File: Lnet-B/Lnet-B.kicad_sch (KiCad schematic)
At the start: 13 parts, among them J601 RJ12, J602 RJ12, Q601 BC847, U601 LM311

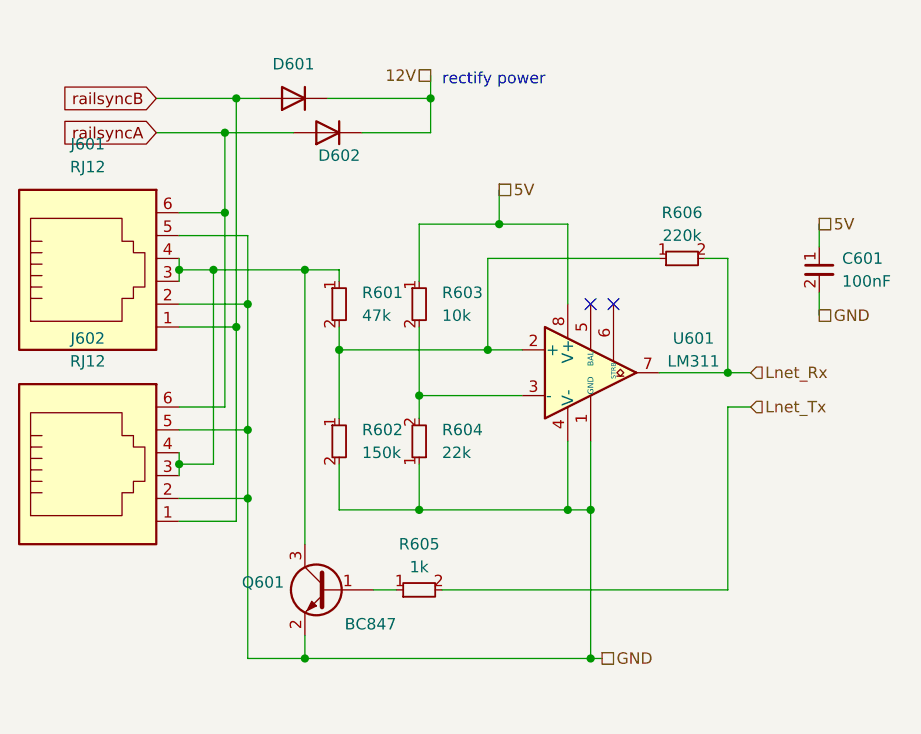
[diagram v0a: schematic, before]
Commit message: removed hierarchial labels for power symbols and replaced them with actual power symbols also updated footprint of the inductor of the 5V buck
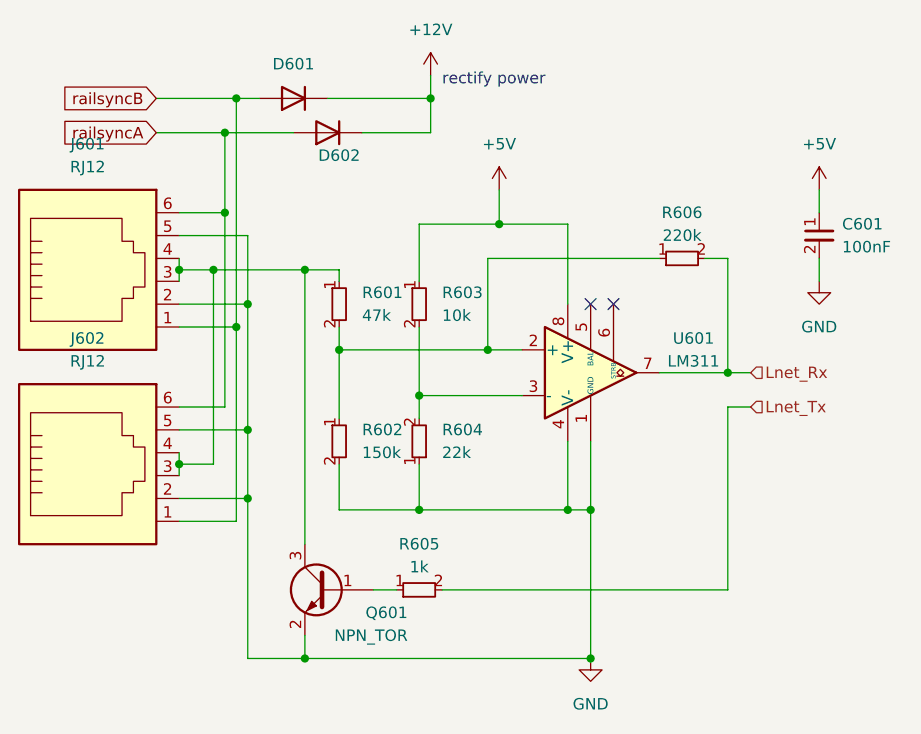
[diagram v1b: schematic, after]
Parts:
- removed Q601: BC847, Package_TO_SOT_SMD:SOT-23, symbol Transistor_BJT:BC847
- added Q601: NPN_TOR, Package_TO_SOT_SMD:SOT-23, symbol custom_kicad_lib_sk:NPN_TOR
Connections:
- net GND: now also Q601.2 (E)
- net at J601.3, J601.4, J602.3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: now also Q601.3 (C)
- net at R605.1: now also Q601.1 (B)
- net 12V renamed +12V
- net 5V renamed +5V
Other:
- moved on the sheet: C601
